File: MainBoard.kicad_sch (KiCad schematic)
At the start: 84 parts, among them J1 Conn_01x04, J10 Conn_01x02, J11 Conn_01x03, J12 Conn_01x03, J13 Conn_01x04, J14 Conn_01x03, J15 Conn_01x04, J16 Conn_01x05, J17 Conn_01x05, J18 Conn_01x06, J19 Conn_01x05, J2 Conn_01x04, J20 Conn_01x08, J21 Conn_01x03, J22 Conn_01x03, J23 Conn_01x05, J24 Conn_01x04, J25 Conn_01x04, J26 Conn_01x04, J27 Conn_01x04, J28 Conn_01x04, J3 Conn_01x06, J4 Conn_01x02, J5 Conn_01x02, J6 Conn_01x02, J7 Conn_01x04, J8 Conn_01x04, J9 Conn_01x02, Q1 NMOS_80A, Q10 NMOS_80A, Q11 NMOS_80A, Q12 NMOS, Q2 NMOS_80A, Q3 NMOS_80A, Q4 NMOS, Q5 NMOS, Q6 NMOS, Q7 NMOS, Q8 NMOS, Q9 NMOS, U1 TJA1051T-3, U10 INA228, U2 INA228, U5 INA228, U6 ESP32-DEVKITC-32D, U7 MCP23017_SO, U8 MCP23017_SO, U9 INA228

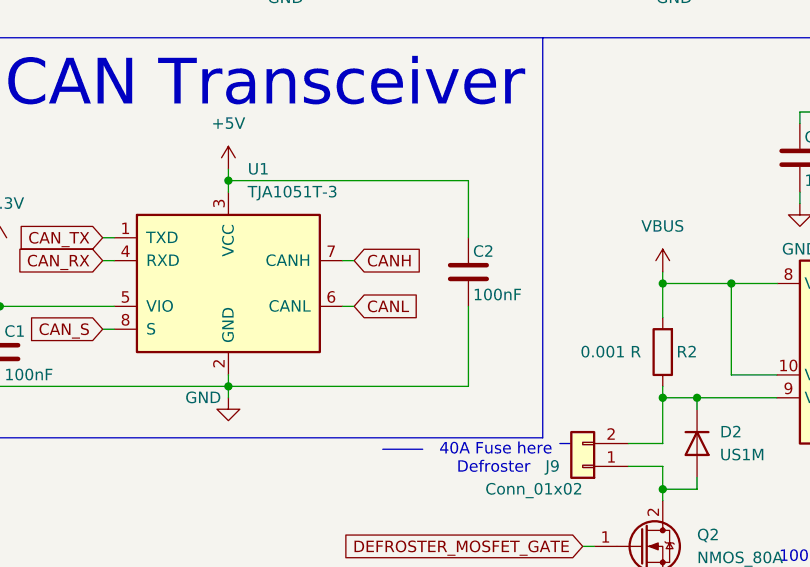
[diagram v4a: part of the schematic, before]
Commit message: added 120 R CAN terminator
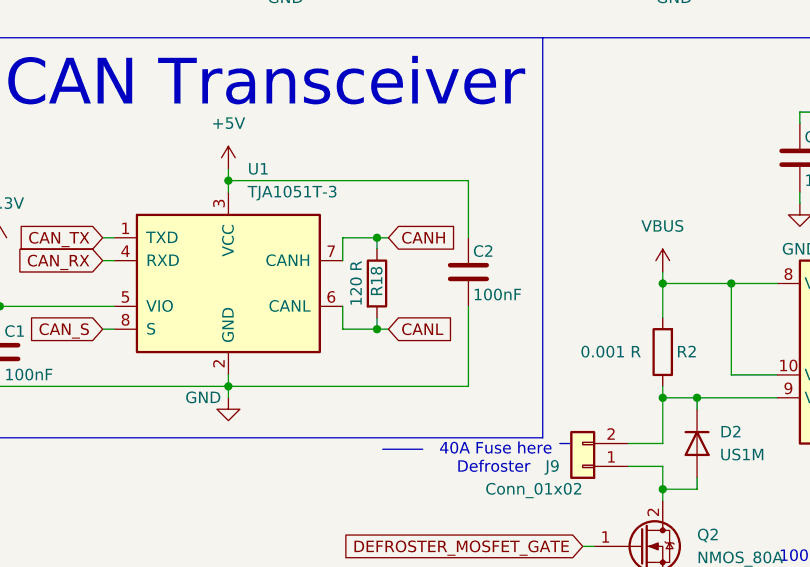
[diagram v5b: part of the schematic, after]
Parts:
- added R18: 120 R, Resistor_SMD:R_1206_3216Metric_Pad1.30x1.75mm_HandSolder, symbol Device:R
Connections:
- net CANH: now also R18.1
- net CANL: now also R18.2
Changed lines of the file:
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@@
 	)
 	(junction
+		(at 57.15 185.42)
+		(diameter 0)
+		(color 0 0 0 0)
+	)
+	(junction
 		(at 210.82 88.9)
 		(diameter 0)
@@
 	)
 	(junction
+		(at 57.15 195.58)
+		(diameter 0)
+		(color 0 0 0 0)
+	)
+	(junction
 		(at 293.37 171.45)
 		(diameter 0)
@@
 	(wire
 		(pts
-			(xy 53.34 187.96) (xy 54.61 187.96)
+			(xy 53.34 185.42) (xy 57.15 185.42)
 		)
 		(stroke
@@
 	(wire
 		(pts
+			(xy 57.15 185.42) (xy 58.42 185.42)
+		)
+		(stroke
+			(width 0)
+			(type default)
+		)
+	)
+	(wire
+		(pts
 			(xy 264.16 161.29) (xy 261.62 161.29)
 		)
@@
 	(wire
 		(pts
+			(xy 57.15 194.31) (xy 57.15 195.58)
+		)
+		(stroke
+			(width 0)
+			(type default)
+		)
+	)
+	(wire
+		(pts
 			(xy 326.39 184.15) (xy 322.58 184.15)
 		)
@@
 	(wire
 		(pts
+			(xy 57.15 195.58) (xy 58.42 195.58)
+		)
+		(stroke
+			(width 0)
+			(type default)
+		)
+	)
+	(wire
+		(pts
 			(xy 293.37 110.49) (xy 293.37 111.76)
 		)
@@
 	(wire
 		(pts
+			(xy 53.34 185.42) (xy 53.34 187.96)
+		)
+		(stroke
+			(width 0)
+			(type default)
+		)
+	)
+	(wire
+		(pts
 			(xy 80.01 219.71) (xy 81.28 219.71)
 		)
@@
 	(wire
 		(pts
+			(xy 53.34 195.58) (xy 53.34 193.04)
+		)
+		(stroke
+			(width 0)
+			(type default)
+		)
+	)
+	(wire
+		(pts
 			(xy 85.09 58.42) (xy 87.63 58.42)
 		)
@@
 	(wire
 		(pts
+			(xy 57.15 185.42) (xy 57.15 186.69)
+		)
+		(stroke
+			(width 0)
+			(type default)
+		)
+	)
+	(wire
+		(pts
 			(xy 297.18 96.52) (xy 297.18 97.79)
 		)
@@
 	(wire
 		(pts
-			(xy 53.34 193.04) (xy 54.61 193.04)
+			(xy 53.34 195.58) (xy 57.15 195.58)
 		)
 		(stroke
@@
 	(global_label "CANH"
 		(shape input)
-		(at 54.61 187.96 0)
+		(at 58.42 185.42 0)
 		(fields_autoplaced yes)
 		(effects
@@
 		)
 		(property "Intersheetrefs" "${INTERSHEET_REFS}"
-			(at 62.6148 187.96 0)
+			(at 66.4248 185.42 0)
 			(effects
 				(font
@@
 	(global_label "CANL"
 		(shape input)
-		(at 54.61 193.04 0)
+		(at 58.42 195.58 0)
 		(fields_autoplaced yes)
 		(effects
@@
 		)
 		(property "Intersheetrefs" "${INTERSHEET_REFS}"
-			(at 62.3124 193.04 0)
+			(at 66.1224 195.58 0)
 			(effects
 				(font
@@
 					(unit 1)
 				)
+			)
+		)
+	)
+	(symbol
+		(lib_id "Device:R")
+		(at 57.15 190.5 0)
+		(unit 1)
+		(exclude_from_sim no)
+		(in_bom yes)
+		(on_board yes)
+		(dnp no)
+		(property "Reference" "R18"
+			(at 57.15 190.246 90)
+			(effects
+				(font
+					(size 1.27 1.27)
+				)
+			)
+		)
+		(property "Value" "120 R"
+			(at 54.864 190.5 90)
+			(effects
+				(font
+					(size 1.27 1.27)
+				)
+			)
+		)
+		(property "Footprint" "Resistor_SMD:R_1206_3216Metric_Pad1.30x1.75mm_HandSolder"
+			(at 55.372 190.5 90)
+			(effects
+				(font
+					(size 1.27 1.27)
+				)
+				(hide yes)
+			)
+		)
+		(property "Datasheet" "~"
+			(at 57.15 190.5 0)
+			(effects
+				(font
+					(size 1.27 1.27)
+				)
+				(hide yes)
+			)
+		)
+		(property "Description" "Resistor"
+			(at 57.15 190.5 0)
+			(effects
+				(font
+					(size 1.27 1.27)
+				)
+				(hide yes)
+			)
+		)
+		(pin "1"
+		)
+		(pin "2"
+		)
+		(instances
+			(project "MainBoard"
+				(path "/6deb7572-40fc-4be3-9f80-b7a356c09b38"
+					(reference "R18")
+					(unit 1)
+				)
